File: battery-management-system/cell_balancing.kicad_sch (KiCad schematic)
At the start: 30 parts, among them J22 BALANCE_INPUTS, J23 BALANCE_CURRENT, J27 BALANCE_CONTROL, Q11 DMN3404L, Q12 DMN3730U, Q14 DMN3730U, Q15 DMN3730U, Q16 DMN3730U, Q17 DMN3730U, SW1 CELL1_MINUS, SW2 CELL1_PLUS, SW3 CELL2_MINUS, SW4 CELL2_PLUS, SW5 CELL3_PLUS, SW6 CELL3_MINUS, SW7 CELL4_PLUS, SW8 CELL4_MINUS, U13 MC74VHC139

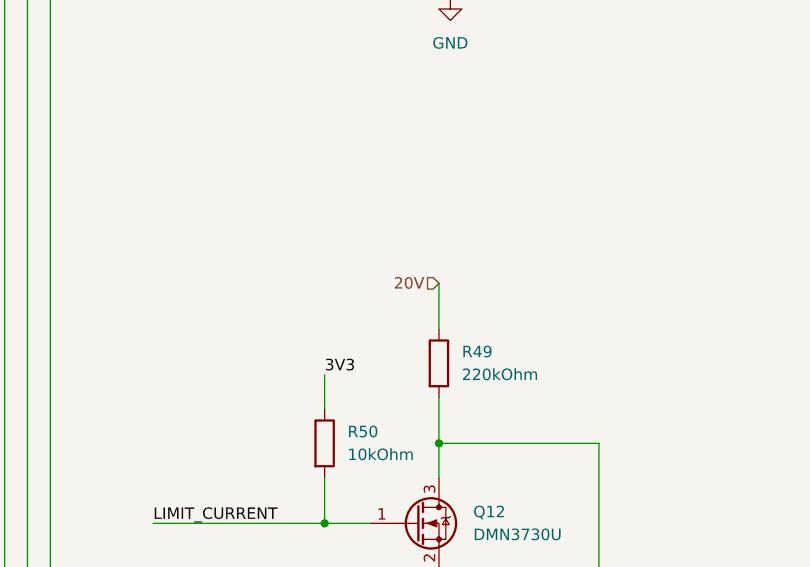
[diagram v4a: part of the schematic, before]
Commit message: add negative power supply for OPAMPs
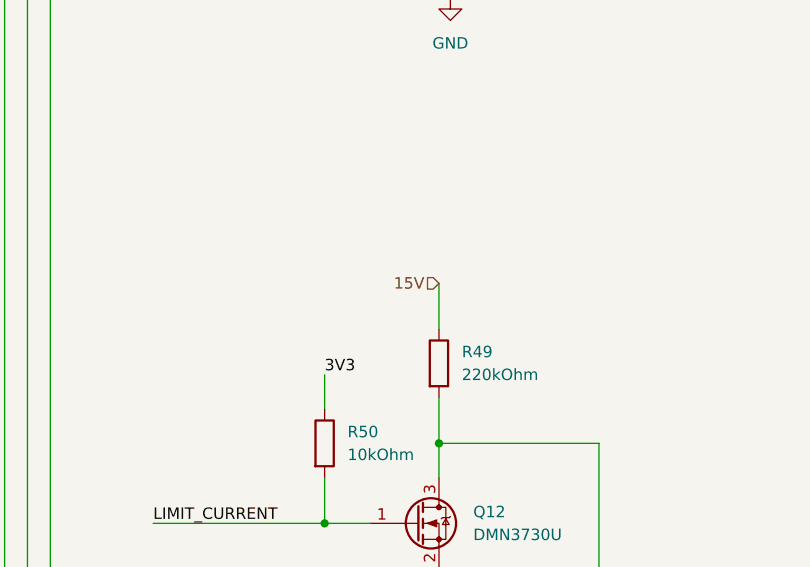
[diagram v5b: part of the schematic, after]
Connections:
- net 20V renamed 15V
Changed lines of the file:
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@@
     (effects (font (size 1.27 1.27)) (justify right))
   )
-  (hierarchical_label "20V" (shape input) (at 143.51 93.98 180) (fields_autoplaced)
+  (hierarchical_label "15V" (shape input) (at 143.51 93.98 180) (fields_autoplaced)
     (effects (font (size 1.27 1.27)) (justify right))
   )

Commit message: implement negative power supply for OPAMPs
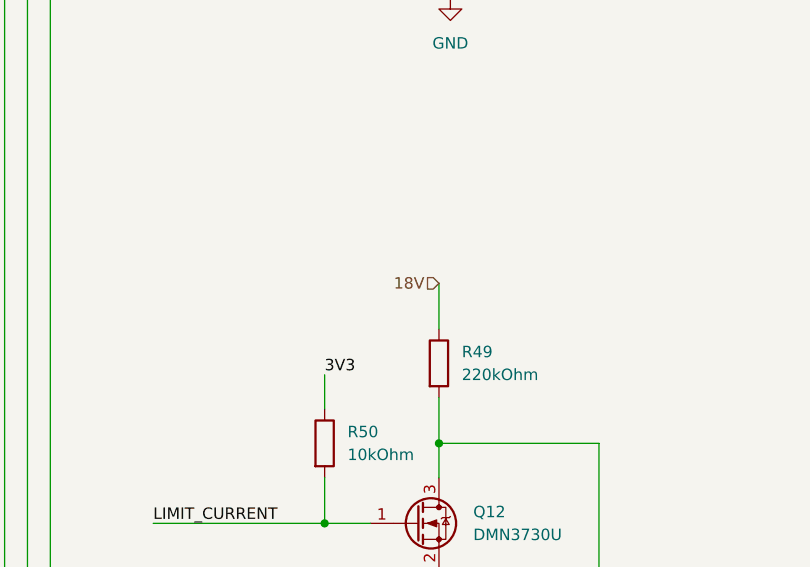
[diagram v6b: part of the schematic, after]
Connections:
- net 15V renamed 18V
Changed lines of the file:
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@@
     (effects (font (size 1.27 1.27)) (justify right))
   )
-  (hierarchical_label "15V" (shape input) (at 143.51 93.98 180) (fields_autoplaced)
+  (hierarchical_label "18V" (shape input) (at 143.51 93.98 180) (fields_autoplaced)
     (effects (font (size 1.27 1.27)) (justify right))
   )

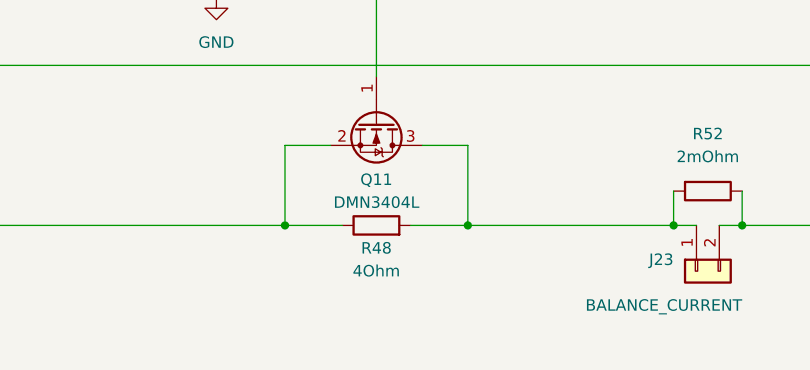
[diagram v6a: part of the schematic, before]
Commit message: fix PCB errors
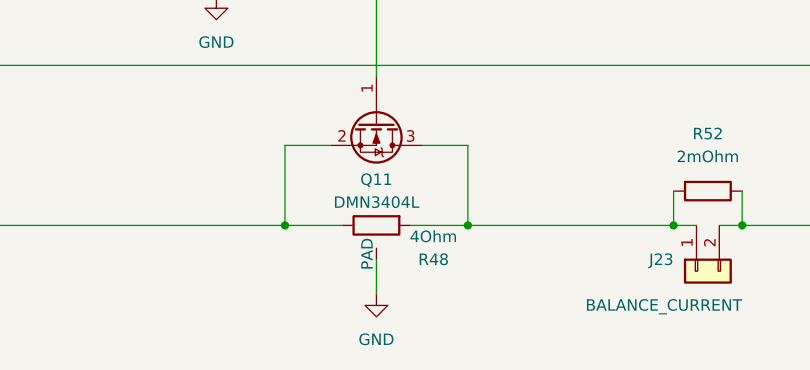
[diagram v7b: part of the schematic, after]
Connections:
- net GND: now also R48.3 (PAD)
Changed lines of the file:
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@@
+    (stroke (width 0) (type default))
+  )
+  (wire (pts (xy 161.29 158.75) (xy 161.29 162.56))
     (stroke (width 0) (type default))
   )
@@
     )
   )
+  (symbol (lib_id "power:GND") (at 161.29 162.56 0) (unit 1)
+    (in_bom yes) (on_board yes) (dnp no) (fields_autoplaced)
+    (property "Reference" "#PWR043" (at 161.29 168.91 0)
+      (effects (font (size 1.27 1.27)) hide)
+    )
+    (property "Value" "GND" (at 161.29 167.64 0)
+      (effects (font (size 1.27 1.27)))
+    )
+    (property "Footprint" "" (at 161.29 162.56 0)
+      (effects (font (size 1.27 1.27)) hide)
+    )
+    (property "Datasheet" "" (at 161.29 162.56 0)
+      (effects (font (size 1.27 1.27)) hide)
+    )
+    (pin "1")
+    (instances
+      (project "battery-management-system"
+        (path "/5272f0ff-3069-41a9-bca2-80beede8b4b2/3d1b4e38-a765-486c-a970-a0d54d5b41d9"
+          (reference "#PWR043") (unit 1)
+        )
+      )
+    )
+  )
   (symbol (lib_id "power:GND") (at 200.66 49.53 0) (unit 1)
     (in_bom yes) (on_board yes) (dnp no) (fields_autoplaced)
@@
     )
   )
-  (symbol (lib_id "benediktibk:R_4Ohm_SMD_35W_1%") (at 161.29 154.94 90) (unit 1)
+  (symbol (lib_id "benediktibk:R_4Ohm_SMD_35W_1%") (at 161.29 154.94 90) (mirror x) (unit 1)
     (in_bom yes) (on_board yes) (dnp no)
-    (property "Reference" "R48" (at 161.29 157.48 90)
-      (effects (font (size 1.27 1.27)))
-    )
-    (property "Value" "4Ohm" (at 161.29 160.02 90)
-      (effects (font (size 1.27 1.27)))
-    )
-    (property "Footprint" "benediktibk:TO-263-resistor" (at 160.782 165.1 90)
+    (property "Reference" "R48" (at 167.64 158.75 90)
+      (effects (font (size 1.27 1.27)))
+    )
+    (property "Value" "4Ohm" (at 167.64 156.21 90)
+      (effects (font (size 1.27 1.27)))
+    )
+    (property "Footprint" "benediktibk:TO-263-resistor" (at 160.782 144.78 90)
       (effects (font (size 1.27 1.27)) hide)
     )
@@
       (effects (font (size 1.27 1.27)) hide)
     )
-    (property "RS order number" " 796-2431" (at 160.02 172.72 0)
+    (property "RS order number" " 796-2431" (at 160.02 137.16 0)
       (effects (font (size 1.27 1.27)) hide)
     )
     (pin "2")
     (pin "1")
-    (instances
-      (project "battery-management-system"
+    (pin "3")
+    (instances
+      (project "battery-management-system"

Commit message: place and route
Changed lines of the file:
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@@
-    (stroke (width 0) (type default))
-  )
-  (wire (pts (xy 222.25 25.4) (xy 226.06 25.4))
     (stroke (width 0) (type default))
   )
@@
     (stroke (width 0) (type default))
   )
-  (wire (pts (xy 222.25 19.05) (xy 226.06 19.05))
+  (wire (pts (xy 222.25 19.05) (xy 229.87 19.05))
     (stroke (width 0) (type default))
   )
@@
     (stroke (width 0) (type default))
   )
+  (wire (pts (xy 222.25 25.4) (xy 229.87 25.4))
+    (stroke (width 0) (type default))
+  )
   (wire (pts (xy 72.39 118.11) (xy 87.63 118.11))
     (stroke (width 0) (type default))
@@
     (stroke (width 0) (type default))
   )
+  (wire (pts (xy 246.38 17.78) (xy 246.38 22.86))
+    (stroke (width 0) (type default))
+  )
   (wire (pts (xy 143.51 106.68) (xy 143.51 111.76))
     (stroke (width 0) (type default))
@@
     (effects (font (size 1.27 1.27)) (justify left bottom))
   )
-  (label "3V3" (at 226.06 25.4 0) (fields_autoplaced)
+  (label "3V3" (at 229.87 25.4 0) (fields_autoplaced)
     (effects (font (size 1.27 1.27)) (justify left bottom))
   )
@@
     (effects (font (size 1.27 1.27)) (justify left bottom))
   )
-  (label "5V" (at 226.06 19.05 0) (fields_autoplaced)
+  (label "5V" (at 229.87 19.05 0) (fields_autoplaced)
     (effects (font (size 1.27 1.27)) (justify left bottom))
   )
@@
   (hierarchical_label "SELECT_A1" (shape input) (at 194.31 59.69 180) (fields_autoplaced)
     (effects (font (size 1.27 1.27)) (justify right))
+  )
+  (netclass_flag "" (length 2.54) (shape round) (at 215.9 154.94 0) (fields_autoplaced)
+    (effects (font (size 1.27 1.27)) (justify left bottom))
+    (property "Netclass" "1A" (at 216.5985 152.4 0)
+      (effects (font (size 1.27 1.27) italic) (justify left))
+    )
+  )
+  (netclass_flag "" (length 2.54) (shape round) (at 142.24 154.94 0) (fields_autoplaced)
+    (effects (font (size 1.27 1.27)) (justify left bottom))
+    (property "Netclass" "1A" (at 142.9385 152.4 0)
+      (effects (font (size 1.27 1.27) italic) (justify left))
+    )
+  )
+  (netclass_flag "" (length 2.54) (shape round) (at 214.63 137.16 0) (fields_autoplaced)
+    (effects (font (size 1.27 1.27)) (justify left bottom))
+    (property "Netclass" "1A" (at 215.3285 134.62 0)
+      (effects (font (size 1.27 1.27) italic) (justify left))
+    )
+  )
+  (netclass_flag "" (length 2.54) (shape round) (at 261.62 109.22 180) (fields_autoplaced)
+    (effects (font (size 1.27 1.27)) (justify right bottom))
+    (property "Netclass" "CONTROL_SIGNAL" (at 262.3185 111.76 0)
+      (effects (font (size 1.27 1.27) italic) (justify left))
+    )
+  )
+  (netclass_flag "" (length 2.54) (shape round) (at 261.62 85.09 180) (fields_autoplaced)
+    (effects (font (size 1.27 1.27)) (justify right bottom))
+    (property "Netclass" "CONTROL_SIGNAL" (at 262.3185 87.63 0)
+      (effects (font (size 1.27 1.27) italic) (justify left))
+    )
+  )
+  (netclass_flag "" (length 2.54) (shape round) (at 184.15 154.94 0) (fields_autoplaced)
+    (effects (font (size 1.27 1.27)) (justify left bottom))
+    (property "Netclass" "1A" (at 184.8485 152.4 0)
+      (effects (font (size 1.27 1.27) italic) (justify left))
+    )
+  )
+  (netclass_flag "" (length 2.54) (shape round) (at 246.38 17.78 0) (fields_autoplaced)
+    (effects (font (size 1.27 1.27)) (justify left bottom))
+    (property "Netclass" "SUPPLY" (at 247.0785 15.24 0)
+      (effects (font (size 1.27 1.27) italic) (justify left))
+    )
+  )
+  (netclass_flag "" (length 2.54) (shape round) (at 261.62 60.96 180) (fields_autoplaced)
+    (effects (font (size 1.27 1.27)) (justify right bottom))
+    (property "Netclass" "CONTROL_SIGNAL" (at 262.3185 63.5 0)
+      (effects (font (size 1.27 1.27) italic) (justify left))
+    )
+  )
+  (netclass_flag "" (length 2.54) (shape round) (at 261.62 36.83 180) (fields_autoplaced)
+    (effects (font (size 1.27 1.27)) (justify right bottom))
+    (property "Netclass" "CONTROL_SIGNAL" (at 262.3185 39.37 0)
+      (effects (font (size 1.27 1.27) italic) (justify left))
+    )
   )
   (symbol (lib_id "benediktibk:DMN3730U") (at 245.11 91.44 0) (unit 1)
@@
         )
       )
+    )
+  )
+  (symbol (lib_id "power:GND") (at 246.38 22.86 0) (unit 1)
+    (in_bom yes) (on_board yes) (dnp no) (fields_autoplaced)
+    (property "Reference" "#PWR048" (at 246.38 29.21 0)
+      (effects (font (size 1.27 1.27)) hide)
+    )
+    (property "Value" "GND" (at 246.38 27.94 0)
+      (effects (font (size 1.27 1.27)))
+    )
+    (property "Footprint" "" (at 246.38 22.86 0)
+      (effects (font (size 1.27 1.27)) hide)
+    )
+    (property "Datasheet" "" (at 246.38 22.86 0)
+      (effects (font (size 1.27 1.27)) hide)
+    )
+    (pin "1")
+    (instances
+      (project "battery-management-system"
+        (path "/5272f0ff-3069-41a9-bca2-80beede8b4b2/3d1b4e38-a765-486c-a970-a0d54d5b41d9"
+          (reference "#PWR048") (unit 1)
+        )
+      )
